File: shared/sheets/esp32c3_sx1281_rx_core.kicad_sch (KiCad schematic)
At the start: 0 parts

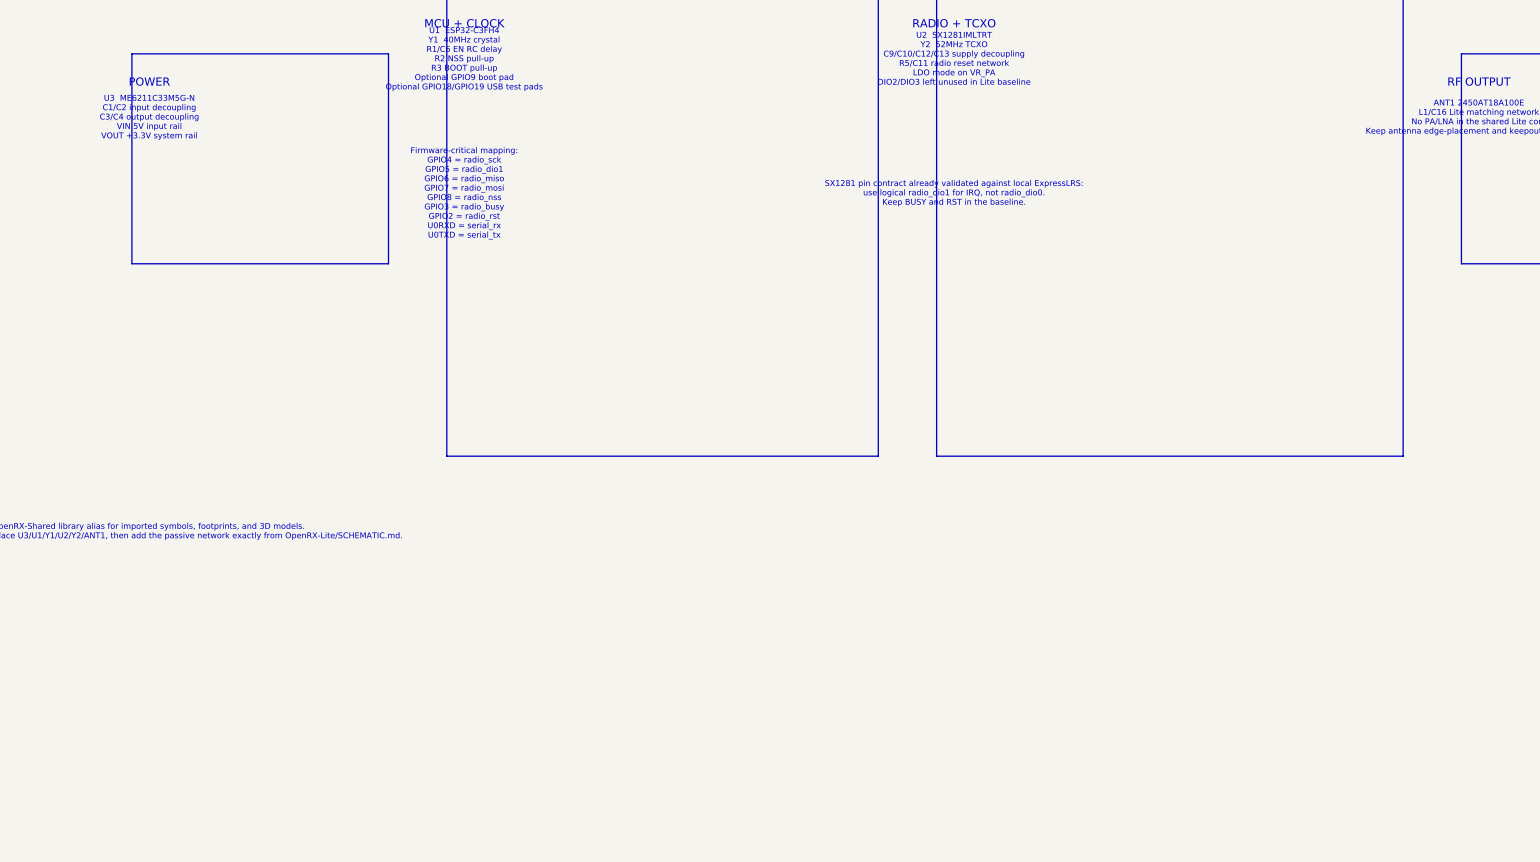
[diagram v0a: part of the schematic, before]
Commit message: Update all DESIGN.md: TLV75533 X2SON LDO, XL-1010 1x1mm LED
- Lite/Nano/900/Dual: ME6211 SOT-23-5 → TLV75533PDQNR X2SON-4 (1x1mm)
- Gemini: keeps AP2112K (600mA needed for dual radios)
- PWM: keeps AMS1117 (needs >6V input range)
- All: WS2812B-2020 → XL-1010RGBC-WS2812B (1x1mm)
- Updated cap values for TLV755 (1uF local + 10uF bulk)
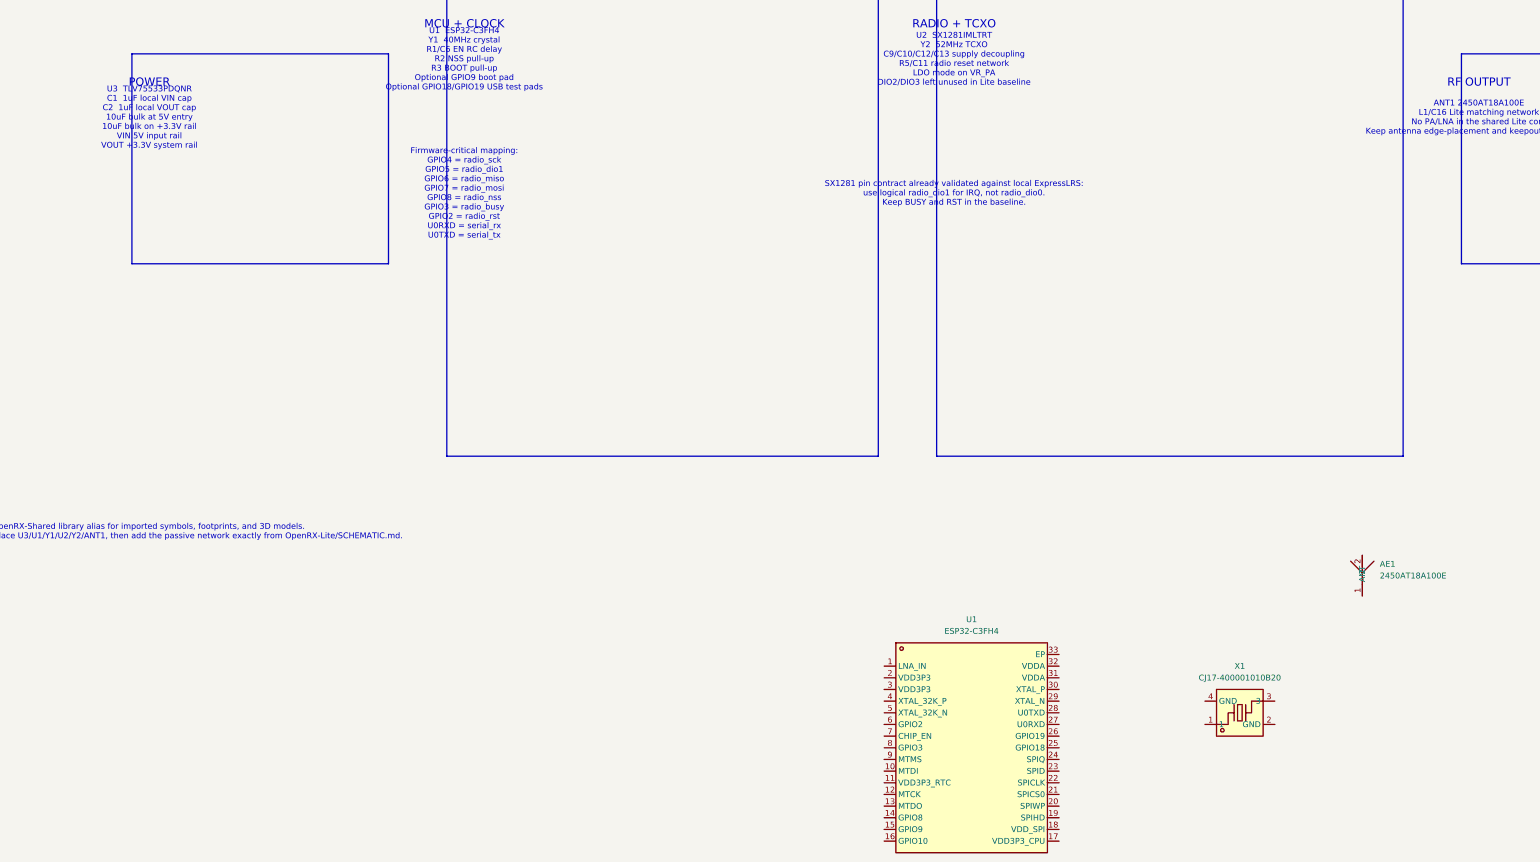
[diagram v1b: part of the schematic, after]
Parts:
- added AE1: 2450AT18A100E, OpenRX-Shared:ANT-SMD_L3.2-W1.6, symbol OpenRX-Shared:2450AT18A100E
- added U1: ESP32-C3FH4, OpenRX-Shared:QFN-32_L5.0-W5.0-P0.50-TL-EP3.7, symbol OpenRX-Shared:ESP32-C3FH4
- added X1: CJ17-400001010B20, OpenRX-Shared:CRYSTAL-SMD_4P-L1.6-W1.2-BL, symbol OpenRX-Shared:CJ17-400001010B20
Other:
- note added: "U3 TLV75533PDQNR C1 1uF local VIN cap C2 1uF local VOUT cap 10uF bulk at 5V entry 10uF bulk on +3.3V rail VIN 5V input rail VOUT +3.3V system rail"
- note removed: "U3 ME6211C33M5G-N C1/C2 input decoupling C3/C4 output decoupling VIN 5V input rail VOUT +3.3V system rail"
